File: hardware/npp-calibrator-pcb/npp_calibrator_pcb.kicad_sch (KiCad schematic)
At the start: 7 parts, among them X1 SOIC16 Test Socket, X2 DE9_Plug, X3 DE9_Plug

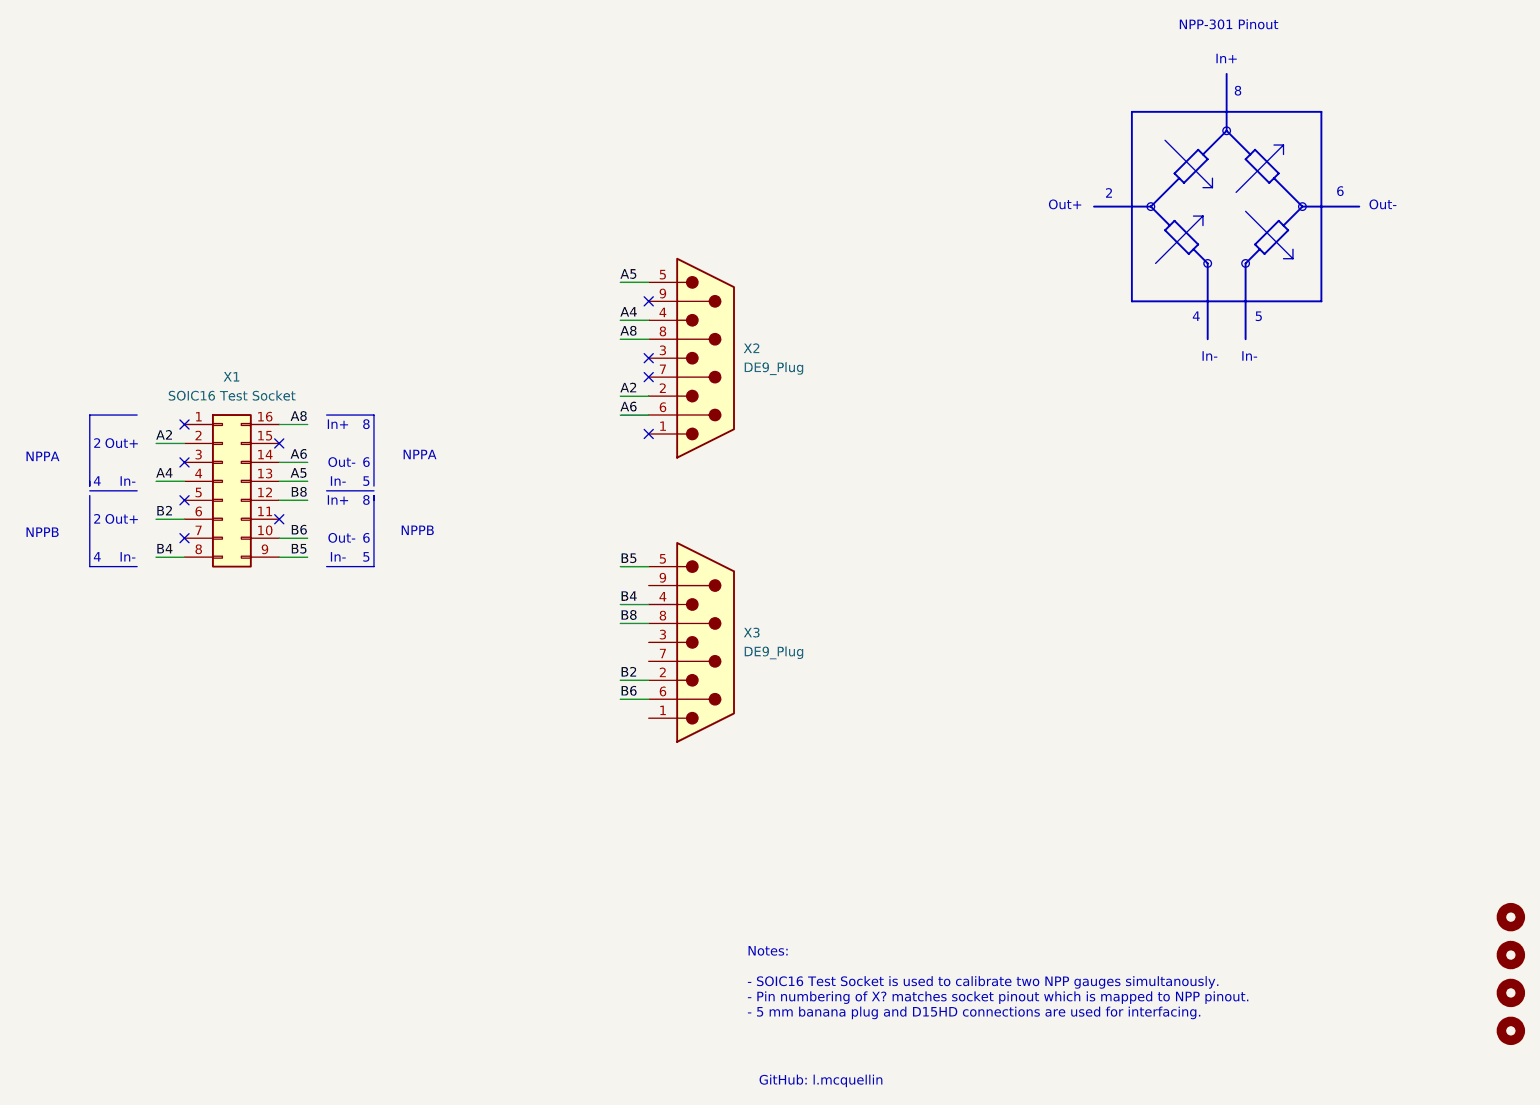
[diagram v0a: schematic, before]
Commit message: Updates to calibration hardware
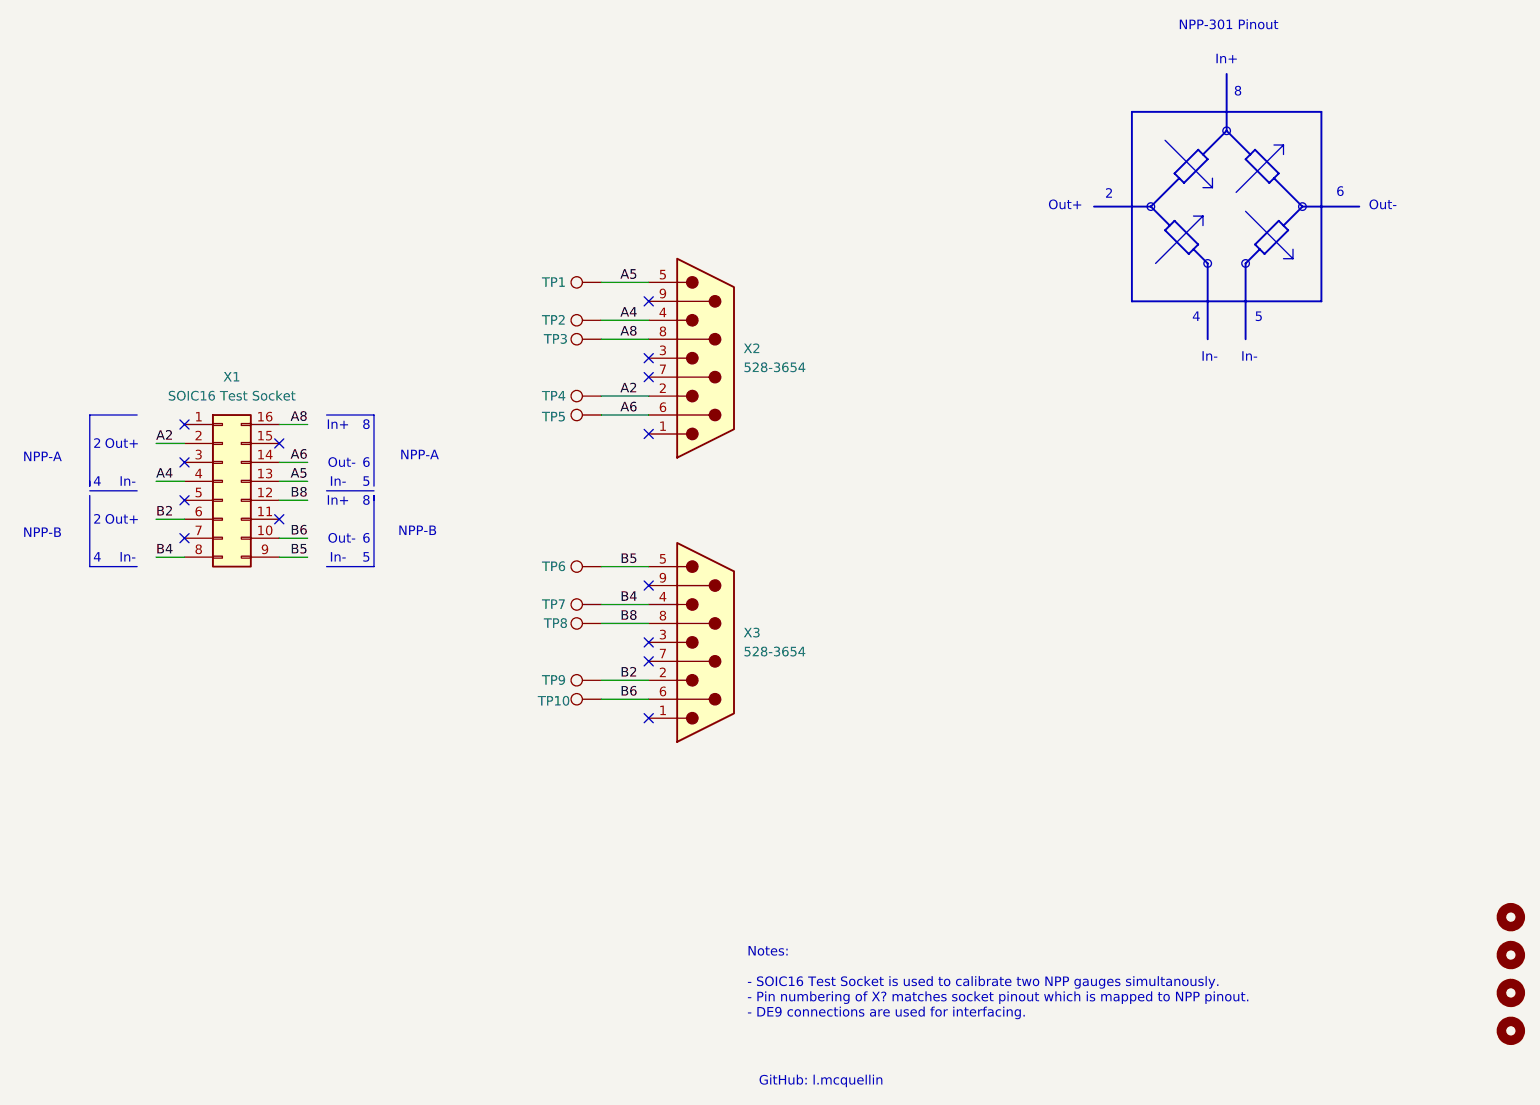
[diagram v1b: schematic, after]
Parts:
- added TP1, TP10, TP2, TP3, TP4, TP5, TP6, TP7, TP8, TP9: TestPoint, TestPoint:TestPoint_Pad_D2.0mm, symbol Connector:TestPoint
- X1: footprint Socket:SOIC_Socket_16_SOCKET-SOICN-16-1.27 -> NPP_Calbrator:PA-SOCKET-SOICN-16-1.27
- X2, X3: value DE9_Plug -> 528-3654; footprint Connector_Dsub:DSUB-9_Male_Horizontal_P2.77x2.84mm_EdgePinOffset4.94mm_Housed_MountingHolesOffset4.94mm -> Connector_Dsub:DSUB-9_Male_Horizontal_P2.77x2.84mm_EdgePinOffset9.40mm
- renumbered H4 to H1, H3 to H2, H2 to H3, H1 to H4
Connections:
- net A2: now also TP4.1
- net A4: now also TP2.1
- net A5: now also TP1.1
- net A6: now also TP5.1
- net A8: now also TP3.1
- net B2: now also TP9.1
- net B4: now also TP7.1
- net B5: now also TP6.1
- net B6: now also TP10.1
- net B8: now also TP8.1
- no-connect marks 10 -> 14
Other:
- note added: "NPP-A"
- note added: "NPP-B"
- note added: "Notes: - SOIC16 Test Socket is used to calibrate two NPP gauges simultanously. - Pin numbering of X? matches socket pinout which is mapped to NPP pinout. - DE9 connections are used for interfacing."
- note removed: "NPPA"
- note removed: "NPPB"
- note removed: "Notes: - SOIC16 Test Socket is used to calibrate two NPP gauges simultanously. - Pin numbering of X? matches socket pinout which is mapped to NPP pinout. - 5 mm banana plug and D15HD connections are used for interfacing."
